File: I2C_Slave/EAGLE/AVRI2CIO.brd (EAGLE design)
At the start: 99.1 x 78.7 mm, 39 parts, among them IC1 MEGA8-P

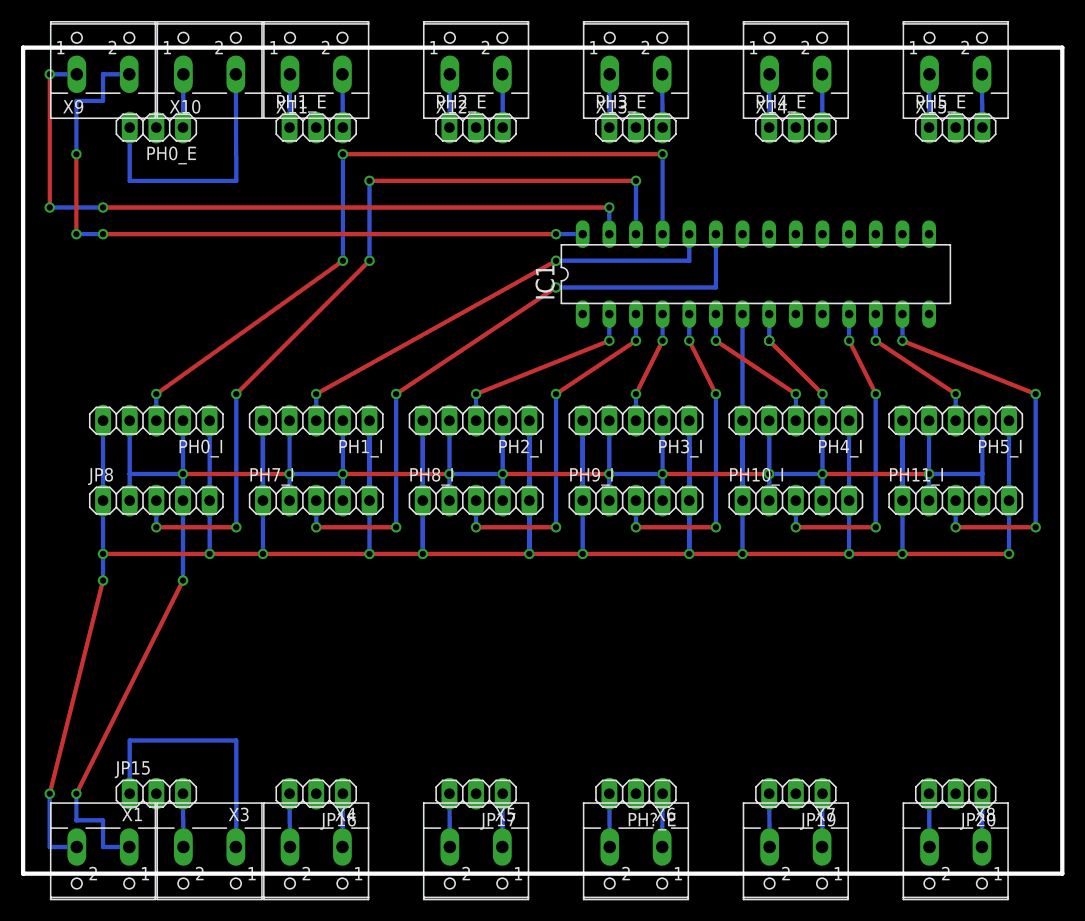
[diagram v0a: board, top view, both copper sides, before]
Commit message: modify eagle item names
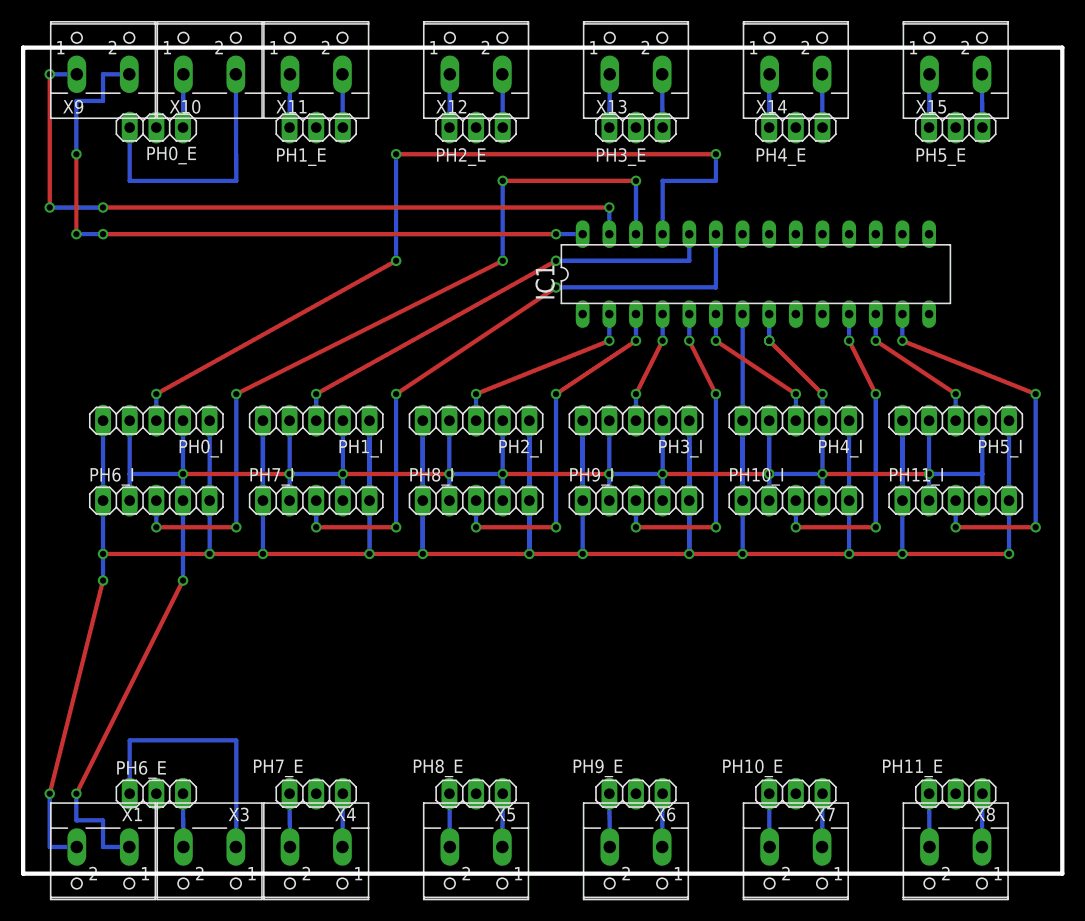
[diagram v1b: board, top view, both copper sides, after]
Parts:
- renumbered JP15 to PH6_E, JP16 to PH7_E, JP17 to PH8_E, JP19 to PH10_E, JP20 to PH11_E, JP8 to PH6_I, PH?_E to PH9_E
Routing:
- net PC2: track 72.6 -> 82.0 mm
- net PC3: track 78.9 -> 76.7 mm
